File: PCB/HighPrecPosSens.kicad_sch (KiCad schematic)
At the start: 81 parts, among them J1 Conn_01x02_Male, J2 Conn_01x02_Male, J3 Conn_01x02_Male, J4 Conn_01x02_Male, J5 Conn_01x06_Male, U1 ST1S14PHR, U2 S12443, U3 LM393DR2G, U4 LM393DR2G, U5 74LVC541A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

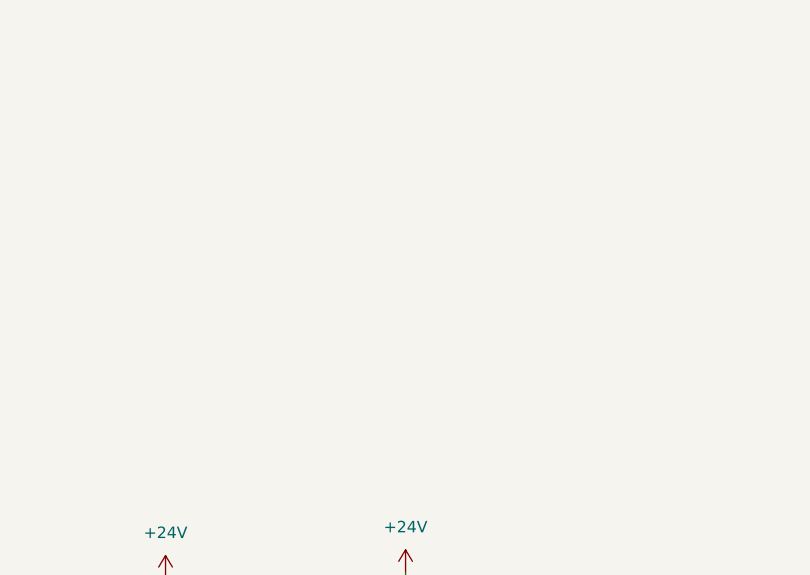
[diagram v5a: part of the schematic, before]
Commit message: some mounting holes added
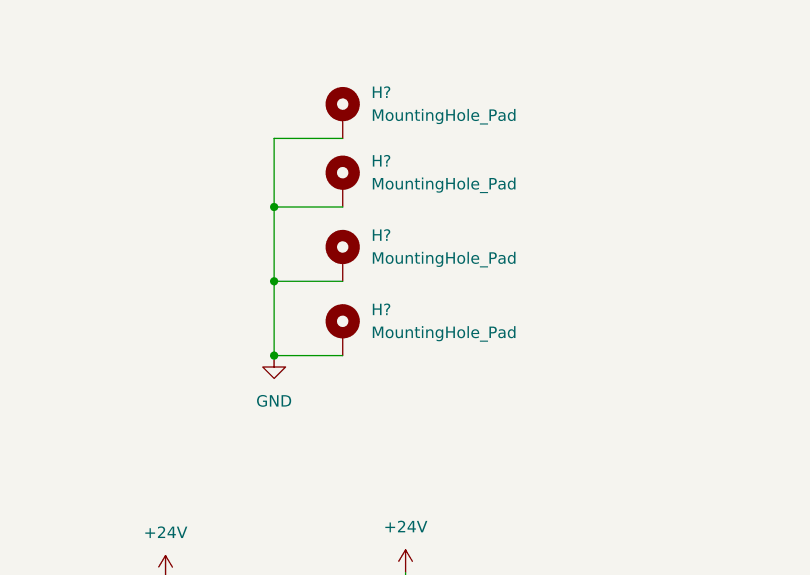
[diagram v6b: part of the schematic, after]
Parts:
- added H? (x4): MountingHole_Pad, MountingHole:MountingHole_3.2mm_M3_Pad, symbol Mechanical:MountingHole_Pad
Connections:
- net GND: now also H?.1, H?.1, H?.1, H?.1
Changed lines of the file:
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@@
   (junction (at 276.86 193.675) (diameter 0) (color 0 0 0 0)
   )
+  (junction (at 56.515 43.18) (diameter 0) (color 0 0 0 0)
+  )
   (junction (at 99.06 261.62) (diameter 0) (color 0 0 0 0)
   )
@@
   (junction (at 276.86 162.56) (diameter 0) (color 0 0 0 0)
   )
+  (junction (at 56.515 34.925) (diameter 0) (color 0 0 0 0)
+  )
+  (junction (at 56.515 51.435) (diameter 0) (color 0 0 0 0)
+  )
   (junction (at 212.725 177.165) (diameter 0) (color 0 0 0 0)
   )
@@
     (stroke (width 0) (type default) (color 0 0 0 0))
   )
+  (wire (pts (xy 64.135 51.435) (xy 56.515 51.435))
+    (stroke (width 0) (type default) (color 0 0 0 0))
+  )
   (wire (pts (xy 386.08 34.925) (xy 386.08 172.72))
     (stroke (width 0) (type default) (color 0 0 0 0))
@@
     (stroke (width 0) (type default) (color 0 0 0 0))
   )
+  (wire (pts (xy 56.515 51.435) (xy 56.515 43.18))
+    (stroke (width 0) (type default) (color 0 0 0 0))
+  )
   (wire (pts (xy 211.709 86.995) (xy 211.709 99.695))
     (stroke (width 0) (type default) (color 0 0 0 0))
@@
     (stroke (width 0) (type default) (color 0 0 0 0))
   )
+  (wire (pts (xy 56.515 27.305) (xy 56.515 34.925))
+    (stroke (width 0) (type default) (color 0 0 0 0))
+  )
   (wire (pts (xy 237.49 64.135) (xy 237.49 64.77))
     (stroke (width 0) (type default) (color 0 0 0 0))
@@
     (stroke (width 0) (type default) (color 0 0 0 0))
   )
+  (wire (pts (xy 64.135 27.305) (xy 56.515 27.305))
+    (stroke (width 0) (type default) (color 0 0 0 0))
+  )
   (wire (pts (xy 259.08 81.915) (xy 282.702 81.915))
     (stroke (width 0) (type default) (color 0 0 0 0))
@@
     (stroke (width 0) (type default) (color 0 0 0 0))
   )
+  (wire (pts (xy 64.135 43.18) (xy 56.515 43.18))
+    (stroke (width 0) (type default) (color 0 0 0 0))
+  )
   (wire (pts (xy 212.09 213.995) (xy 207.01 213.995))
     (stroke (width 0) (type default) (color 0 0 0 0))
@@
     (stroke (width 0) (type default) (color 0 0 0 0))
   )
+  (wire (pts (xy 56.515 34.925) (xy 64.135 34.925))
+    (stroke (width 0) (type default) (color 0 0 0 0))
+  )
   (wire (pts (xy 296.545 112.395) (xy 296.545 99.695))
     (stroke (width 0) (type default) (color 0 0 0 0))
@@
     (stroke (width 0) (type default) (color 0 0 0 0))
   )
+  (wire (pts (xy 56.515 43.18) (xy 56.515 34.925))
+    (stroke (width 0) (type default) (color 0 0 0 0))
+  )
   (wire (pts (xy 121.92 193.04) (xy 144.145 193.04))
     (stroke (width 0) (type default) (color 0 0 0 0))
@@
     (pin "1")
   )
+  (symbol (lib_name "GND_3") (lib_id "power:GND") (at 56.515 51.435 0) (unit 1)
+    (in_bom yes) (on_board yes) (fields_autoplaced)
+    (property "Reference" "#PWR?" (id 0) (at 56.515 57.785 0)
+      (effects (font (size 1.27 1.27)) hide)
+    )
+    (property "Value" "GND" (id 1) (at 56.515 56.515 0))
+    (property "Footprint" "" (id 2) (at 56.515 51.435 0)
+      (effects (font (size 1.27 1.27)) hide)
+    )
+    (property "Datasheet" "" (id 3) (at 56.515 51.435 0)
+      (effects (font (size 1.27 1.27)) hide)
+    )
+    (pin "1")
+  )
   (symbol (lib_id "Device:LED") (at 44.45 142.24 90) (unit 1)
     (in_bom yes) (on_board yes) (fields_autoplaced)
@@
     (pin "8")
   )
+  (symbol (lib_id "Mechanical:MountingHole_Pad") (at 64.135 32.385 0) (unit 1)
+    (in_bom yes) (on_board yes) (fields_autoplaced)
+    (property "Reference" "H?" (id 0) (at 67.31 29.8449 0)
+      (effects (font (size 1.27 1.27)) (justify left))
+    )
+    (property "Value" "MountingHole_Pad" (id 1) (at 67.31 32.3849 0)
+      (effects (font (size 1.27 1.27)) (justify left))
+    )
+    (property "Footprint" "MountingHole:MountingHole_3.2mm_M3_Pad" (id 2) (at 64.135 32.385 0)
+      (effects (font (size 1.27 1.27)) hide)
+    )
+    (property "Datasheet" "~" (id 3) (at 64.135 32.385 0)
+      (effects (font (size 1.27 1.27)) hide)
+    )
+    (property "Mounting" "DNP" (id 9) (at 64.135 32.385 0)
+      (effects (font (size 1.27 1.27)) hide)
+    )
+    (pin "1")
+  )
   (symbol (lib_id "power:+3.3V") (at 231.14 172.085 0) (unit 1)
     (in_bom yes) (on_board yes) (fields_autoplaced)
@@
     (pin "2")
   )
+  (symbol (lib_id "Mechanical:MountingHole_Pad") (at 64.135 40.64 0) (unit 1)
+    (in_bom yes) (on_board yes) (fields_autoplaced)
+    (property "Reference" "H?" (id 0) (at 67.31 38.0999 0)
+      (effects (font (size 1.27 1.27)) (justify left))
+    )
+    (property "Value" "MountingHole_Pad" (id 1) (at 67.31 40.6399 0)
+      (effects (font (size 1.27 1.27)) (justify left))
+    )
+    (property "Footprint" "MountingHole:MountingHole_3.2mm_M3_Pad" (id 2) (at 64.135 40.64 0)
+      (effects (font (size 1.27 1.27)) hide)
+    )
+    (property "Datasheet" "~" (id 3) (at 64.135 40.64 0)
+      (effects (font (size 1.27 1.27)) hide)
+    )
+    (property "Mounting" "DNP" (id 9) (at 64.135 40.64 0)
+      (effects (font (size 1.27 1.27)) hide)
+    )
+    (pin "1")
+  )
   (symbol (lib_id "Device:R") (at 276.86 130.175 180) (unit 1)
     (in_bom yes) (on_board yes)
@@
     (pin "2")
   )
+  (symbol (lib_id "Mechanical:MountingHole_Pad") (at 64.135 48.895 0) (unit 1)
+    (in_bom yes) (on_board yes) (fields_autoplaced)
+    (property "Reference" "H?" (id 0) (at 67.31 46.3549 0)
+      (effects (font (size 1.27 1.27)) (justify left))
+    )
+    (property "Value" "MountingHole_Pad" (id 1) (at 67.31 48.8949 0)
+      (effects (font (size 1.27 1.27)) (justify left))
+    )
+    (property "Footprint" "MountingHole:MountingHole_3.2mm_M3_Pad" (id 2) (at 64.135 48.895 0)
+      (effects (font (size 1.27 1.27)) hide)
+    )
+    (property "Datasheet" "~" (id 3) (at 64.135 48.895 0)
+      (effects (font (size 1.27 1.27)) hide)
+    )
+    (property "Mounting" "DNP" (id 9) (at 64.135 48.895 0)
+      (effects (font (size 1.27 1.27)) hide)
+    )
+    (pin "1")
+  )
   (symbol (lib_id "Connector:Conn_01x06_Male") (at 116.84 193.04 0) (unit 1)
     (in_bom yes) (on_board yes) (fields_autoplaced)
@@
     (pin "1")
   )
+  (symbol (lib_id "Mechanical:MountingHole_Pad") (at 64.135 24.765 0) (unit 1)
+    (in_bom yes) (on_board yes) (fields_autoplaced)
+    (property "Reference" "H?" (id 0) (at 67.31 22.2249 0)
+      (effects (font (size 1.27 1.27)) (justify left))
+    )
+    (property "Value" "MountingHole_Pad" (id 1) (at 67.31 24.7649 0)
+      (effects (font (size 1.27 1.27)) (justify left))
+    )
+    (property "Footprint" "MountingHole:MountingHole_3.2mm_M3_Pad" (id 2) (at 64.135 24.765 0)
+      (effects (font (size 1.27 1.27)) hide)
+    )
+    (property "Datasheet" "~" (id 3) (at 64.135 24.765 0)
+      (effects (font (size 1.27 1.27)) hide)
+    )
+    (property "Mounting" "DNP" (id 9) (at 64.135 24.765 0)
+      (effects (font (size 1.27 1.27)) hide)
+    )
+    (pin "1")
+  )
   (symbol (lib_id "power:+3.3V") (at 363.22 161.29 0) (unit 1)
     (in_bom yes) (on_board yes)
@@
       (reference "#PWR0104") (unit 1) (value "GND") (footprint "")
     )
+    (path "/0dd7dee9-a19e-40f5-92fc-3bb6245e2c70"
+      (reference "#PWR?") (unit 1) (value "GND") (footprint "")
+    )
     (path "/6f052ed9-6923-4aad-9ce7-77a831335223"
       (reference "C1") (unit 1) (value "100n") (footprint "Capacitor_SMD:C_0603_1608Metric")
@@
       (reference "FID4") (unit 1) (value "Fiducial") (footprint "Fiducial:Fiducial_1mm_Mask2mm")
     )
+    (path "/2e4d5ac6-38f9-4500-bf48-9501c64ee03e"
+      (reference "H?") (unit 1) (value "MountingHole_Pad") (footprint "MountingHole:MountingHole_3.2mm_M3_Pad")
+    )
+    (path "/82df9250-4165-47dc-b1f7-05adb7a466ed"
+      (reference "H?") (unit 1) (value "MountingHole_Pad") (footprint "MountingHole:MountingHole_3.2mm_M3_Pad")
+    )
+    (path "/b196d5b8-e474-4682-9489-9dbbd3f0927b"
+      (reference "H?") (unit 1) (value "MountingHole_Pad") (footprint "MountingHole:MountingHole_3.2mm_M3_Pad")
+    )
+    (path "/cffb5fac-e82d-404f-bf3f-17054244c031"
+      (reference "H?") (unit 1) (value "MountingHole_Pad") (footprint "MountingHole:MountingHole_3.2mm_M3_Pad")
+    )
     (path "/8d7aa37b-4484-4215-9461-6291d9f92a28"
